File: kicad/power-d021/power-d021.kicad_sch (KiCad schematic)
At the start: 9 parts, among them J301 T1_SECONDARY, J302 PVDD_TO_CORE

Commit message: docs(setup): share Headroom per project and record T1 harness connector
- Headroom MCP shared by Claude Code, Codex, Pi and Hermes on .headroom/memory.db;
  local settings and wrapper runtime state ignored.
- T1 secondary harness: 3-way red-black-red, CT centre, matches J301;
  housing family, pitch and current rating still TBD.
- Ignore local JLCPCB plugin output; README index links power-d021.
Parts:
- J301: MPN TBD: mate original T1 harness; >=8 A/pin -> TBD: mate original T1 harness (3-way, red-black-red, pitch 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
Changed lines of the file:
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@@
 (kicad_sch (version 20250114) (generator "eeschema") (paper "A3")
 (title_block (title "PS28 D-021 PVDD RECTIFIER - STUDY ONLY") (rev "A-analog-study"))
-(symbol (lib_id "Connector_Generic:Conn_01x03") (at 50.8 50.8 0) (unit 1) (in_bom yes) (on_board yes) (property "Reference" "J301" (at 50.8 45.72 0) (effects (font (size 1 1)) )) (property "Value" "T1_SECONDARY" (at 50.8 55.879999999999995 0) (effects (font (size 1 1)) )) (property "Footprint" "" (at 50.8 55.879999999999995 0) (effects (font (size 1 1)) (hide yes))) (property "MPN" "TBD: mate original T1 harness; >=8 A/pin" (at 50.8 55.879999999999995 0) (effects (font (size 1 1)) (hide yes))) (property "SelectionStatus" "STUDY; passives/interfaces not selected" (at 50.8 55.879999999999995 0) (effects (font (size 1 1)) (hide yes))) (property "Source" "D-021: unregulated PVDD from T1 CT two-diode rectifier; study only; no hardware sign-off" (at 50.8 55.879999999999995 0) (effects (font (size 1 1)) (hide yes))) (pin "1") (pin "2") (pin "3")(instances (project "power-d021" (path "/0b6d9f24-bdcb-5a0f-9be7-66ab5bf77147" (reference "J301") (unit 1)))))
+(symbol (lib_id "Connector_Generic:Conn_01x03") (at 50.8 50.8 0) (unit 1) (in_bom yes) (on_board yes) (property "Reference" "J301" (at 50.8 45.72 0) (effects (font (size 1 1)) )) (property "Value" "T1_SECONDARY" (at 50.8 55.879999999999995 0) (effects (font (size 1 1)) )) (property "Footprint" "" (at 50.8 55.879999999999995 0) (effects (font (size 1 1)) (hide yes))) (property "MPN" "TBD: mate original T1 harness (3-way, red-black-red, pitch unmeasured); >=8 A/pin" (at 50.8 55.879999999999995 0) (effects (font (size 1 1)) (hide yes))) (property "SelectionStatus" "STUDY; passives/interfaces not selected" (at 50.8 55.879999999999995 0) (effects (font (size 1 1)) (hide yes))) (property "Source" "D-021: unregulated PVDD from T1 CT two-diode rectifier; study only; no hardware sign-off" (at 50.8 55.879999999999995 0) (effects (font (size 1 1)) (hide yes))) (pin "1") (pin "2") (pin "3")(instances (project "power-d021" (path "/0b6d9f24-bdcb-5a0f-9be7-66ab5bf77147" (reference "J301") (unit 1)))))
 (wire (pts (xy 45.72 48.26) (xy 41.91 48.26)) (stroke (width 0) (type default)))
 (label "T1_A" (at 41.91 48.26 0) (effects (font (size .9 .9)) (justify right bottom)))

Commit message: docs(power): record T1 harness pitch and wire rating
Pitch ~4 mm (3.96 mm family), UL AWM 1015 20 AWG 105 C 600 V; header series and per-pin rating stay TBD.
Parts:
- J301: MPN TBD: mate original T1 harness (3-way, red-black-red, pitch 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 -> TBD: mate original T1 harness (3-way, red-black-red, ~3.96 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
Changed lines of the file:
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@@
 (kicad_sch (version 20250114) (generator "eeschema") (paper "A3")
 (title_block (title "PS28 D-021 PVDD RECTIFIER - STUDY ONLY") (rev "A-analog-study"))
-(symbol (lib_id "Connector_Generic:Conn_01x03") (at 50.8 50.8 0) (unit 1) (in_bom yes) (on_board yes) (property "Reference" "J301" (at 50.8 45.72 0) (effects (font (size 1 1)) )) (property "Value" "T1_SECONDARY" (at 50.8 55.879999999999995 0) (effects (font (size 1 1)) )) (property "Footprint" "" (at 50.8 55.879999999999995 0) (effects (font (size 1 1)) (hide yes))) (property "MPN" "TBD: mate original T1 harness (3-way, red-black-red, pitch unmeasured); >=8 A/pin" (at 50.8 55.879999999999995 0) (effects (font (size 1 1)) (hide yes))) (property "SelectionStatus" "STUDY; passives/interfaces not selected" (at 50.8 55.879999999999995 0) (effects (font (size 1 1)) (hide yes))) (property "Source" "D-021: unregulated PVDD from T1 CT two-diode rectifier; study only; no hardware sign-off" (at 50.8 55.879999999999995 0) (effects (font (size 1 1)) (hide yes))) (pin "1") (pin "2") (pin "3")(instances (project "power-d021" (path "/0b6d9f24-bdcb-5a0f-9be7-66ab5bf77147" (reference "J301") (unit 1)))))
+(symbol (lib_id "Connector_Generic:Conn_01x03") (at 50.8 50.8 0) (unit 1) (in_bom yes) (on_board yes) (property "Reference" "J301" (at 50.8 45.72 0) (effects (font (size 1 1)) )) (property "Value" "T1_SECONDARY" (at 50.8 55.879999999999995 0) (effects (font (size 1 1)) )) (property "Footprint" "" (at 50.8 55.879999999999995 0) (effects (font (size 1 1)) (hide yes))) (property "MPN" "TBD: mate original T1 harness (3-way, red-black-red, ~3.96 mm pitch, 20 AWG UL1015); >=8 A/pin" (at 50.8 55.879999999999995 0) (effects (font (size 1 1)) (hide yes))) (property "SelectionStatus" "STUDY; passives/interfaces not selected" (at 50.8 55.879999999999995 0) (effects (font (size 1 1)) (hide yes))) (property "Source" "D-021: unregulated PVDD from T1 CT two-diode rectifier; study only; no hardware sign-off" (at 50.8 55.879999999999995 0) (effects (font (size 1 1)) (hide yes))) (pin "1") (pin "2") (pin "3")(instances (project "power-d021" (path "/0b6d9f24-bdcb-5a0f-9be7-66ab5bf77147" (reference "J301") (unit 1)))))
 (wire (pts (xy 45.72 48.26) (xy 41.91 48.26)) (stroke (width 0) (type default)))
 (label "T1_A" (at 41.91 48.26 0) (effects (font (size .9 .9)) (justify right bottom)))

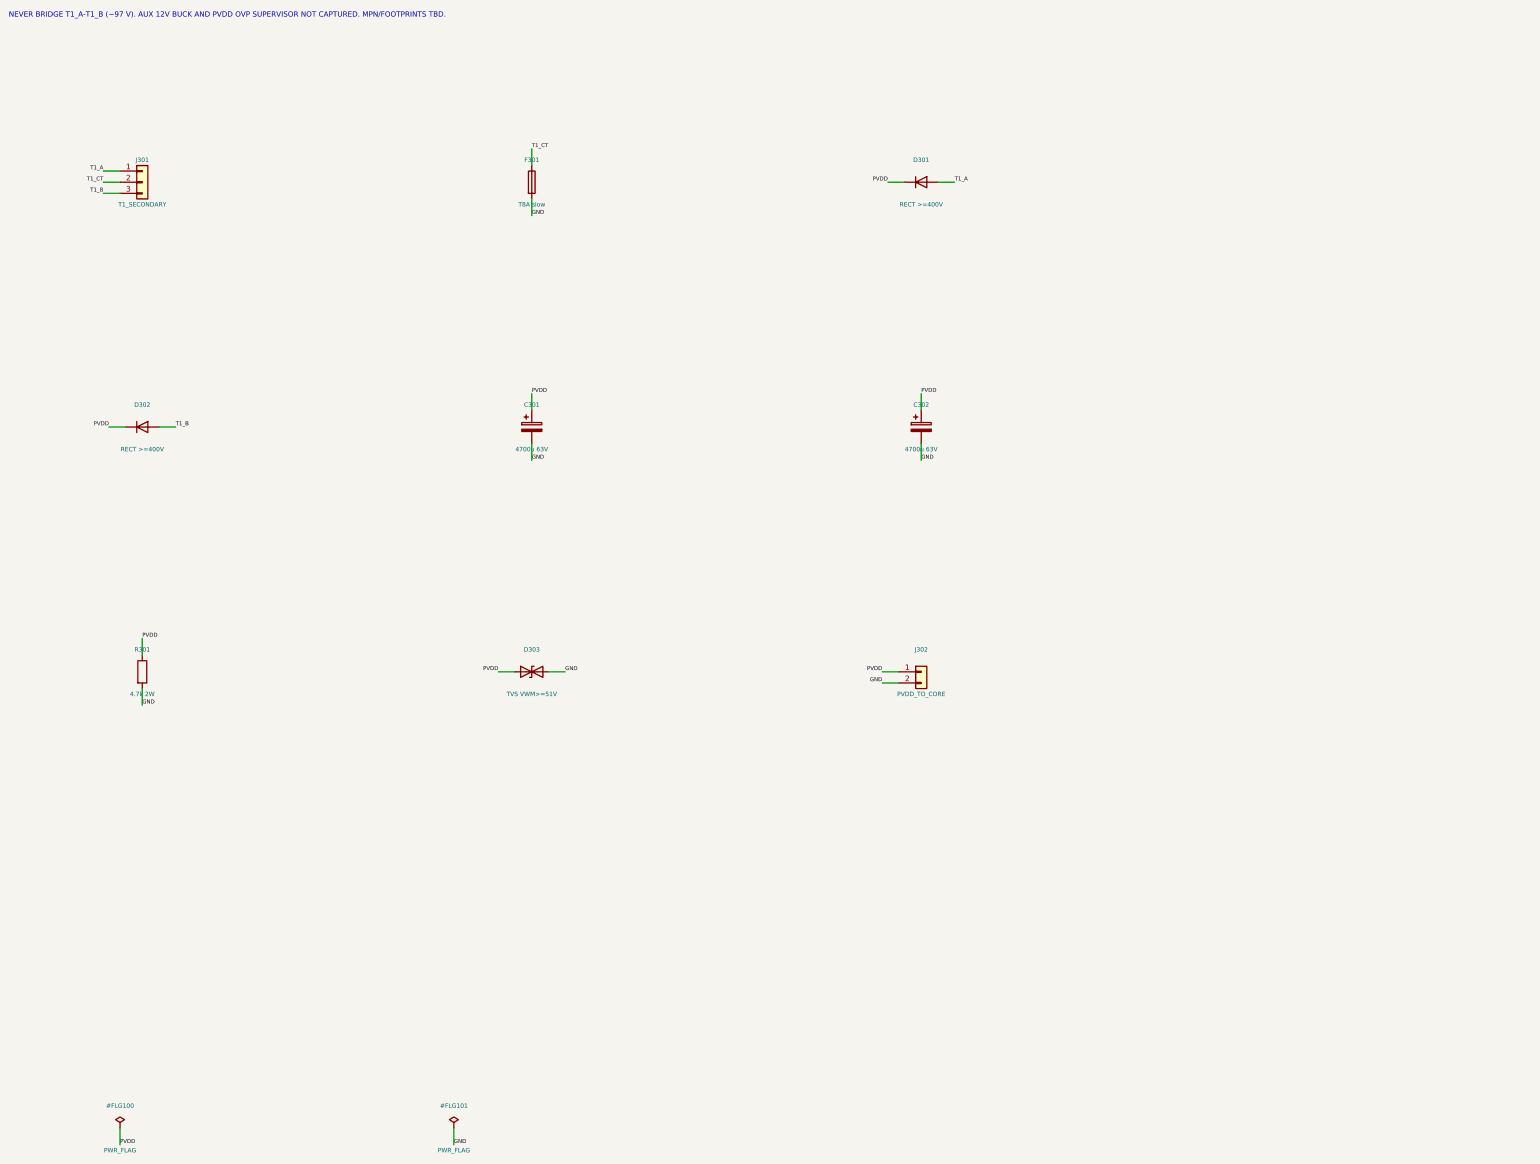
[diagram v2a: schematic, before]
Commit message: feat(power): capture AUX 12 V buck and PVDD window supervisor
- U302 LM5164DDA with TI SNVSAU4D Fig 7-1 values (12.09 V nominal,
  11.69-12.50 V worst case from VREF and 1 % feedback).
- U303 TPS3700DDC window on PVDD: OV 50.97-52.24 V, UV 27.28-28.35 V
  worst case; local symbol from SBVS187G p.4.
- RAILS_OK open-drain wired-AND (PGOOD, OV, UV) for D-020 rails_valid,
  not a direct RESET drive. ERC 0; footprints and some MPNs TBD.
- build() accepts extra local symbols; fetch list adds lm5164/tps3700.
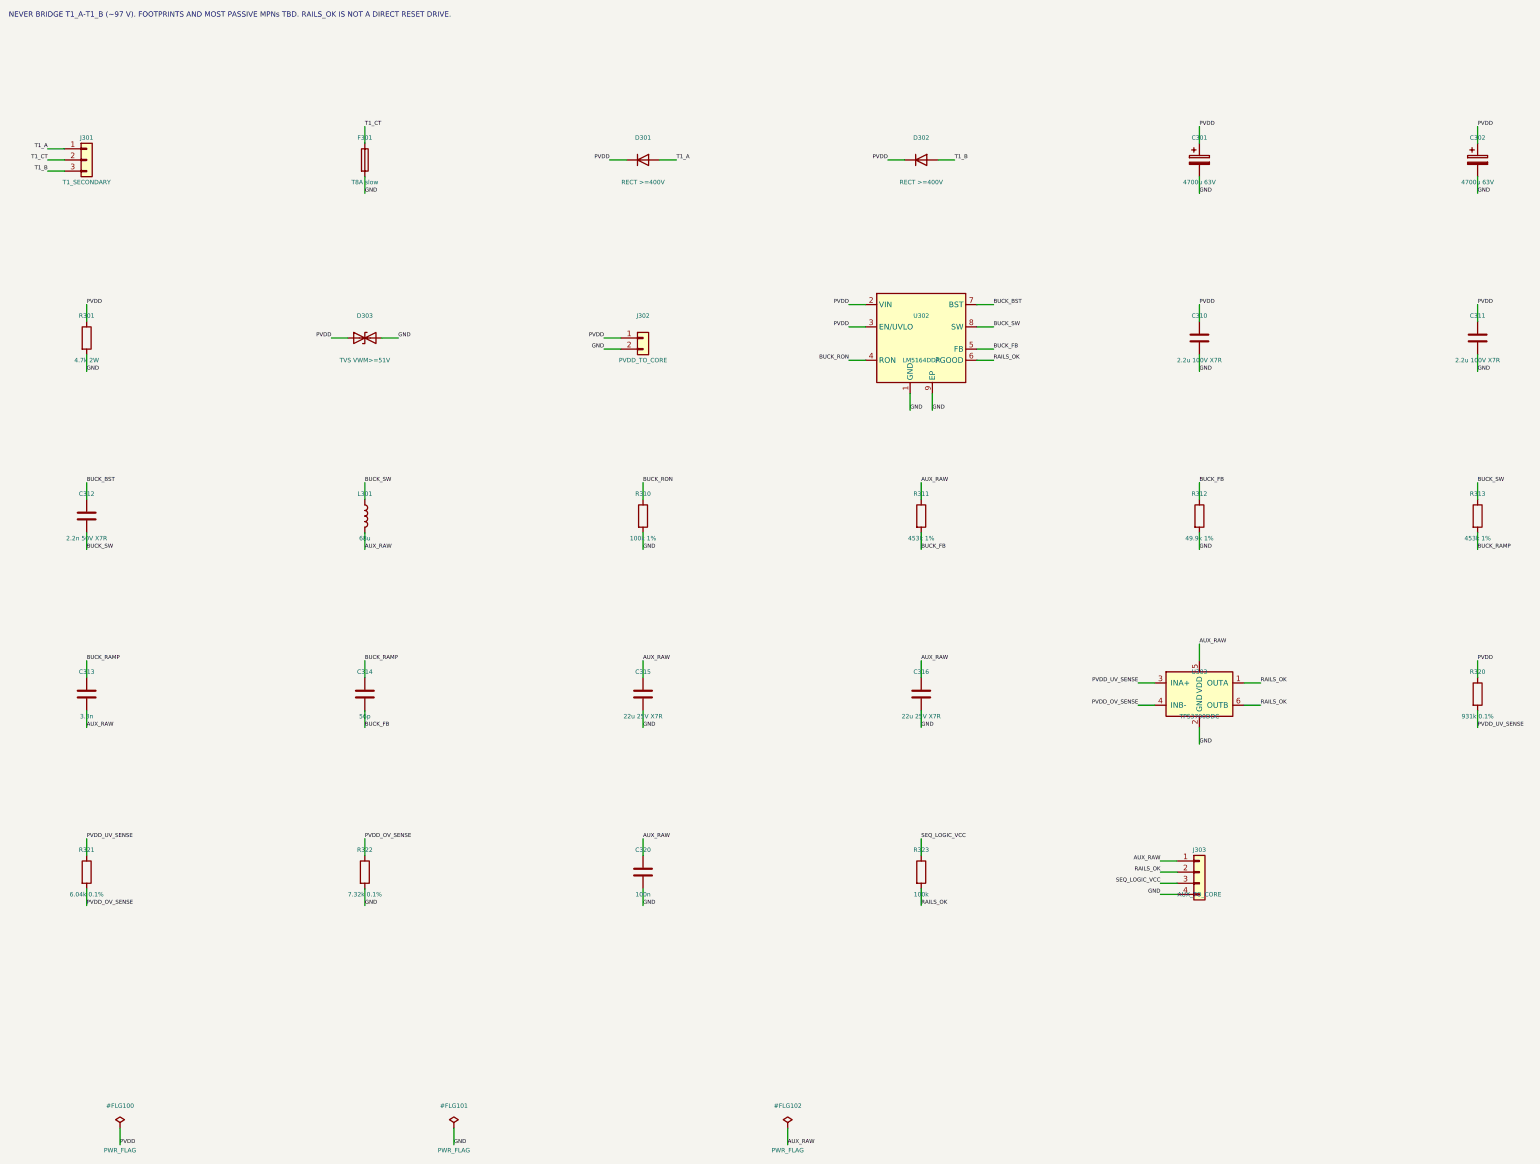
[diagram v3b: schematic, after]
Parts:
- added C310, C311: 2.2u 100V X7R, symbol Device:C
- added C312: 2.2n 50V X7R, symbol Device:C
- added C313: 3.3n, symbol Device:C
- added C314: 56p, symbol Device:C
- added C315, C316: 22u 25V X7R, symbol Device:C
- added C320: 100n, symbol Device:C
- added J303: AUX_TO_CORE, symbol Connector_Generic:Conn_01x04
- added L301: 68u, symbol Device:L
- added R310: 100k 1%, symbol Device:R
- added R311, R313: 453k 1%, symbol Device:R
- added R312: 49.9k 1%, symbol Device:R
- added R320: 931k 0.1%, symbol Device:R
- added R321: 6.04k 0.1%, symbol Device:R
- added R322: 7.32k 0.1%, symbol Device:R
- added R323: 100k, symbol Device:R
- added U302: LM5164DDA, symbol Regulator_Switching:LM5164DDA
- added U303: TPS3700DDC, symbol PS28_POWER:TPS3700DDC
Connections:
- net GND: now also C310.2, C311.2, C315.2, C316.2, C320.2, J303.4 (Pin_4), R310.2, R312.2, R322.2, U302.1 (GND), U302.9 (EP), U303.2 (GND)
- net PVDD: now also C310.1, C311.1, R320.1, U302.2 (VIN), U302.3 (EN/UVLO)
- new net AUX_RAW: C313.2, C315.1, C316.1, C320.1, J303.1 (Pin_1), L301.2, R311.1, U303.5 (VDD)
- new net BUCK_BST: C312.1, U302.7 (BST)
- new net BUCK_FB: C314.2, R311.2, R312.1, U302.5 (FB)
- new net BUCK_RAMP: C313.1, C314.1, R313.2
- new net BUCK_RON: R310.1, U302.4 (RON)
- new net BUCK_SW: C312.2, L301.1, R313.1, U302.8 (SW)
- new net PVDD_OV_SENSE: R321.2, R322.1, U303.4 (INB-)
- new net PVDD_UV_SENSE: R320.2, R321.1, U303.3 (INA+)
- new net RAILS_OK: J303.2 (Pin_2), R323.2, U302.6 (PGOOD), U303.1 (OUTA), U303.6 (OUTB)
- new net SEQ_LOGIC_VCC: J303.3 (Pin_3), R323.1
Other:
- note added: "NEVER BRIDGE T1_A-T1_B (~97 V). FOOTPRINTS AND MOST PASSIVE MPNs TBD. RAILS_OK IS NOT A DIRECT RESET DRIVE."
- note removed: "NEVER BRIDGE T1_A-T1_B (~97 V). AUX 12V BUCK AND PVDD OVP SUPERVISOR NOT CAPTURED. MPN/FOOTPRINTS TBD."
- title: PS28 D-021 PVDD RECTIFIER - STUDY ONLY -> PS28 D-021 POWER - STUDY ONLY
- moved on the sheet: C301, C302, D301, D302, D303, F301, J301, J302, R301

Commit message: feat(eda): capture discrete D-020 sequencer and integrate D-021 power into system candidate
- seq-d020 (D-023): LP2985 3.3 V, two TPS3808 stages (>=360 ms hold),
  74LVC2G74 RUN/ARMED latches (human start edge with CLIP_OTW high, FAULT
  arming and latch with human re-arm), 0.62-1.44 s start timeout, TPS3700
  windows for ANALOG_12V and VMID on the RAILS_OK wired-AND.
- seq_d020_logic simulates the captured netlist; mutation-checked tests.
- system-candidate: power and seq banks outside the OEM outline, 150
  footprints, 421 native pins matched; PVDD_36V renamed PVDD; J4/R7/R8 DNP.
  ERC equal to base (4 PBTL OUT_x, 1 MONO_BIASED), DRC 0, 338 unrouted.
- power-d021: candidate stock footprints, SEQ_3V3 pull-up, manifest restored.
- 3D gallery adds system candidate views framed to show import banks.
- D-019 isolation, discharge, DC sense and mute remain NOT implemented.
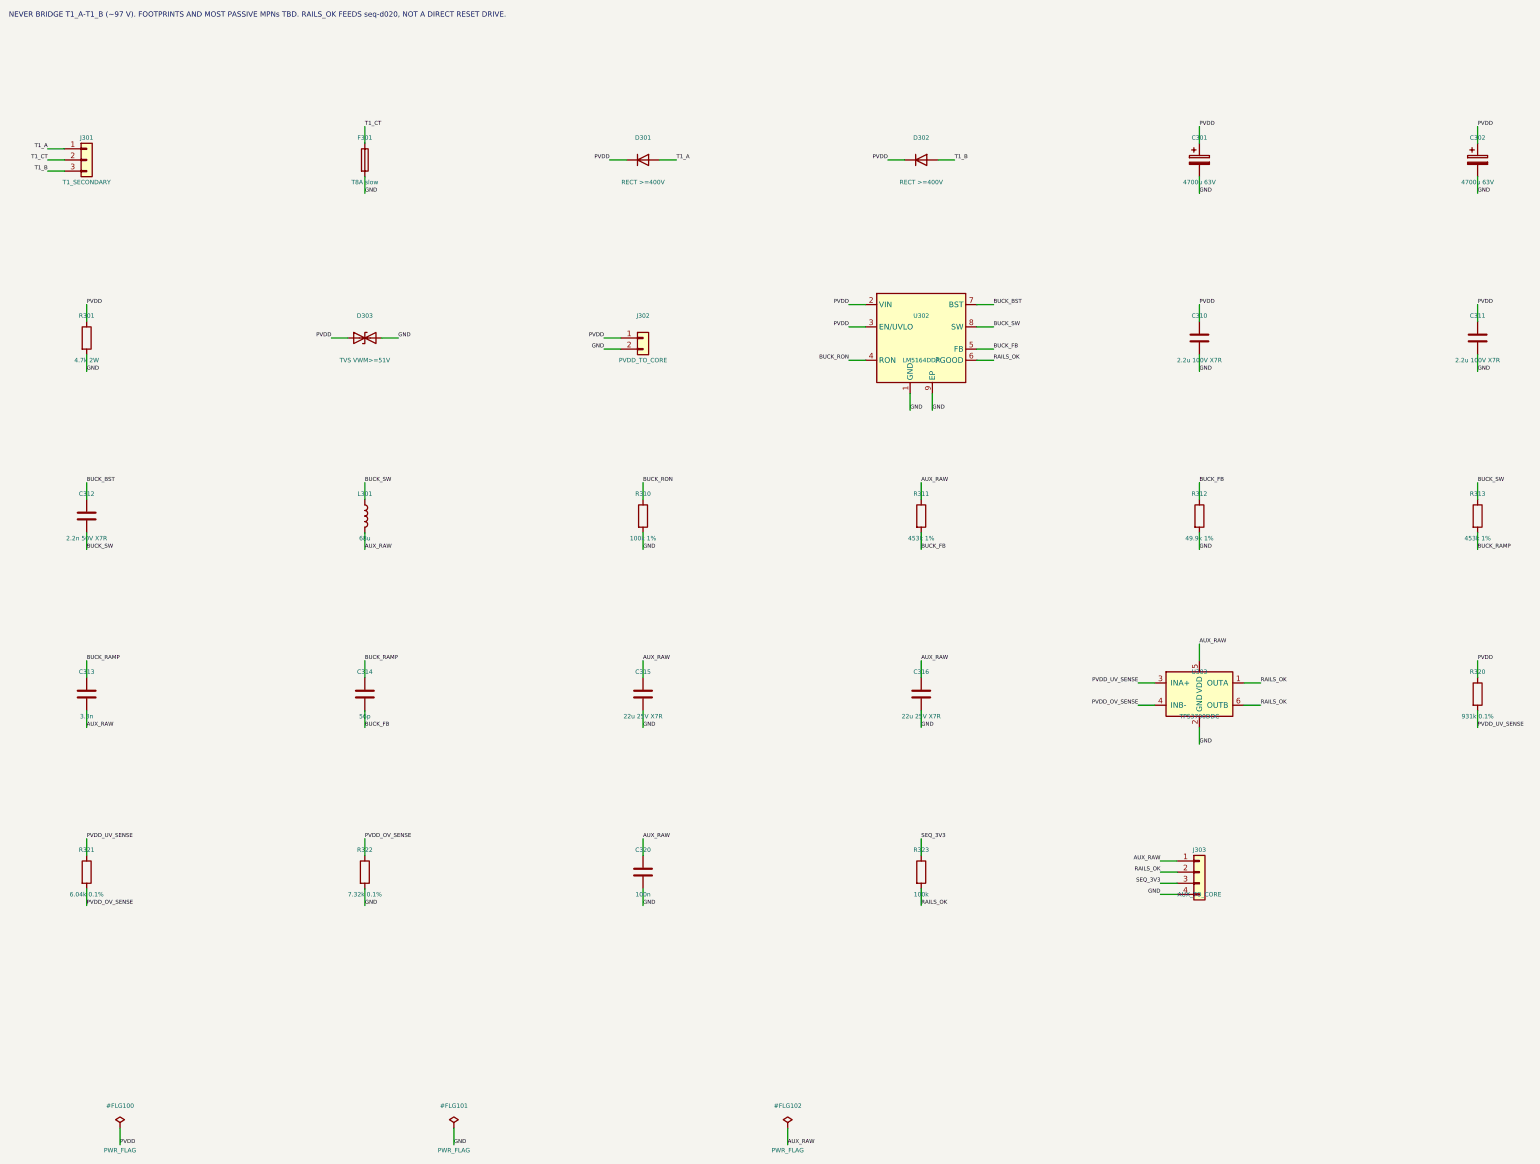
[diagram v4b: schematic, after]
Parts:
- C301, C302: footprint (none) -> Capacitor_THT:CP_Radial_D25.0mm_P10.00mm_SnapIn
- C310, C311, C315, C316: footprint (none) -> Capacitor_SMD:C_1210_3225Metric
- C312: footprint (none) -> Capacitor_SMD:C_0402_1005Metric
- C313, C314, C320: footprint (none) -> Capacitor_SMD:C_0603_1608Metric
- D301, D302: footprint (none) -> Diode_THT:D_P600_R-6_P12.70mm_Horizontal
- D303: footprint (none) -> Diode_SMD:D_SMC
- F301: footprint (none) -> Fuse:Fuseholder_Cylinder-5x20mm_Schurter_0031_8201_Horizontal_Open
- J301: footprint (none) -> Connector_JST:JST_VH_B3P-VH_1x03_P3.96mm_Vertical
- J303: MPN Logical interface: AUX_RAW to core J2, RAILS_OK into D-020 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 -> Logical interface: AUX_RAW to core, RAILS_OK/SEQ_3V3 to seq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
- L301: footprint (none) -> Inductor_SMD:L_Coilcraft_MSS1246T-XXX
- R301: footprint (none) -> Resistor_THT:R_Axial_DIN0414_L11.9mm_D4.5mm_P15.24mm_Horizontal
- R310, R311, R312, R313, R321, R322: footprint (none) -> Resistor_SMD:R_0603_1608Metric
- R320: footprint (none) -> Resistor_SMD:R_1206_3216Metric
- R323: footprint (none) -> Resistor_SMD:R_0603_1608Metric; MPN TBD: pull-up; SEQ_LOGIC_VCC <=14 V (LM5164 PGOOD abs max) -> TBD: pull-up to SEQ_3V3 (seq-d020 LP2985); <=14 V LM5164 PG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
- U302: footprint (none) -> Package_SO:HSOP-8-1EP_3.9x4.9mm_P1.27mm_EP2.41x3.1mm
- U303: footprint (none) -> Package_TO_SOT_SMD:SOT-23-6; MPN TPS3700DDCR (TI SBVS187G p.15 orderable); SOT-23-6 footprin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 -> TPS3700DDCR (TI SBVS187G p.23 package option addendum); SOT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
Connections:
- net SEQ_LOGIC_VCC renamed SEQ_3V3
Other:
- note added: "NEVER BRIDGE T1_A-T1_B (~97 V). FOOTPRINTS AND MOST PASSIVE MPNs TBD. RAILS_OK FEEDS seq-d020, NOT A DIRECT RESET DRIVE."
- note removed: "NEVER BRIDGE T1_A-T1_B (~97 V). FOOTPRINTS AND MOST PASSIVE MPNs TBD. RAILS_OK IS NOT A DIRECT RESET DRIVE."

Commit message: varias ataulizaçoes e correçoes
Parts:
- C301, C302: value 4700u 63V -> 4700u 63V snap-in; MPN TBD: >=63 V, 105 C, ripple >=3.5 A at 120 Hz each -> Rubycon 63USC4700MEFCSN30X30 (LCSC C1498587): 4700 uF/63 V,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
- D301, D302: value RECT >=400V -> MUR3040WTG; MPN TBD: VRRM>=400 V, IF(AV)>=6 A, IFSM>=200 A -> onsemi MUR3040WTG (MUR3020WT/D Rev.7): VRRM 400 V, IF(AV) 1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
- D303: value TVS VWM>=51V -> SMCJ51A; MPN TBD: VWM>=51 V (above 49.8 V worst idle), Vc below 69 V abs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 -> Littelfuse SMCJ51A: VWM 51.0 V, Vc 82.4 V @IPP 18.2 A, PPP 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
- F301: value T8A slow -> T6.3A slow; MPN TBD: time-lag, I2t >= 60 A2s inrush margin, >=63 VDC -> Time-lag (T) 5x20 mm; I2t melt above measured inrush, >=63 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
- J301: MPN TBD: mate original T1 harness (3-way, red-black-red, ~3.96 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 -> JST VH SVH-41T-P1.1 terminals (20-16 AWG, 10 A) on VHR-4N h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
